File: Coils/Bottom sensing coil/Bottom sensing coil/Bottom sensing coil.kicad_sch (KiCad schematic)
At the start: 6 parts, among them J1 Conn_01x02_Socket, J2 Conn_01x02_Pin

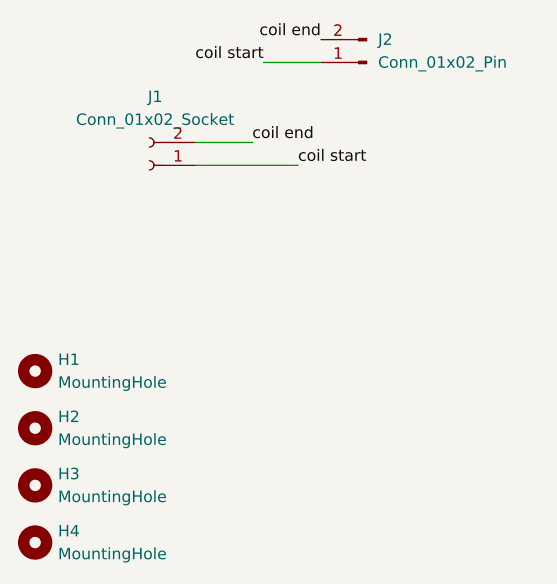
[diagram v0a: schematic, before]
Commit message: added 3d models for OPA3692, THS3091 and BNC connector
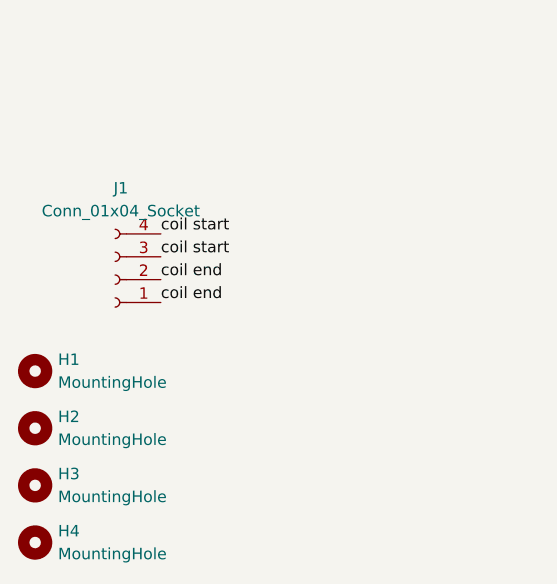
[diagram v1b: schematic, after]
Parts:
- removed J1: Conn_01x02_Socket, Connector_PinSocket_2.54mm:PinSocket_1x02_P2.54mm_Vertical, symbol Connector:Conn_01x02_Socket
- removed J2: Conn_01x02_Pin, Connector_PinHeader_2.54mm:PinHeader_1x02_P2.54mm_Vertical, symbol Connector:Conn_01x02_Pin
- added J1: Conn_01x04_Socket, Connector_PinSocket_2.54mm:PinSocket_1x04_P2.54mm_Horizontal, symbol Connector:Conn_01x04_Socket
- H1, H2, H3, H4: footprint MountingHole:MountingHole_5mm_Pad -> MountingHole:MountingHole_3.2mm_M3_Pad
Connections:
- net coil end: now also J1.1 (Pin_1), J1.2 (Pin_2)
- net coil start: now also J1.3 (Pin_3), J1.4 (Pin_4)
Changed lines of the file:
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@@
 	(generator_version "8.0")
 	(paper "A4")
-	(wire
-		(pts
-			(xy 101.6 55.88) (xy 113.03 55.88)
-		)
-		(stroke
-			(width 0)
-			(type default)
-		)
-	)
-	(wire
-		(pts
-			(xy 115.57 44.45) (xy 109.22 44.45)
-		)
-		(stroke
-			(width 0)
-			(type default)
-		)
-	)
-	(wire
-		(pts
-			(xy 101.6 53.34) (xy 107.95 53.34)
-		)
-		(stroke
-			(width 0)
-			(type default)
-		)
-	)
-	(label "coil end"
-		(at 115.57 41.91 180)
+	(label "coil start"
+		(at 97.79 66.04 0)
 		(fields_autoplaced yes)
 		(effects
@@
 				(size 1.27 1.27)
 			)
-			(justify right bottom)
+			(justify left bottom)
 		)
 	)
 	(label "coil end"
-		(at 107.95 53.34 0)
+		(at 97.79 71.12 0)
 		(fields_autoplaced yes)
 		(effects
@@
 		)
 	)
-	(label "coil start"
-		(at 113.03 55.88 0)
+	(label "coil end"
+		(at 97.79 68.58 0)
 		(fields_autoplaced yes)
 		(effects
@@
 	)
 	(label "coil start"
-		(at 109.22 44.45 180)
+		(at 97.79 63.5 0)
 		(fields_autoplaced yes)
 		(effects
@@
 				(size 1.27 1.27)
 			)
-			(justify right bottom)
+			(justify left bottom)
 		)
 	)
@@
 			)
 		)
-		(property "Footprint" "MountingHole:MountingHole_5mm_Pad"
+		(property "Footprint" "MountingHole:MountingHole_3.2mm_M3_Pad"
 			(at 83.82 91.44 0)
 			(effects
@@
 	)
 	(symbol
-		(lib_id "Connector:Conn_01x02_Pin")
-		(at 120.65 44.45 180)
-		(unit 1)
-		(exclude_from_sim no)
-		(in_bom yes)
-		(on_board yes)
-		(dnp no)
-		(fields_autoplaced yes)
-		(property "Reference" "J2"
-			(at 121.92 41.9099 0)
-			(effects
-				(font
-					(size 1.27 1.27)
-				)
-				(justify right)
-			)
-		)
-		(property "Value" "Conn_01x02_Pin"
-			(at 121.92 44.4499 0)
-			(effects
-				(font
-					(size 1.27 1.27)
-				)
-				(justify right)
-			)
-		)
-		(property "Footprint" "Connector_PinHeader_2.54mm:PinHeader_1x02_P2.54mm_Vertical"
-			(at 120.65 44.45 0)
-			(effects
-				(font
-					(size 1.27 1.27)
-				)
-				(hide yes)
-			)
-		)
-		(property "Datasheet" "~"
-			(at 120.65 44.45 0)
-			(effects
-				(font
-					(size 1.27 1.27)
-				)
-				(hide yes)
-			)
-		)
-		(property "Description" "Generic connector, single row, 01x02, script generated"
-			(at 120.65 44.45 0)
-			(effects
-				(font
-					(size 1.27 1.27)
-				)
-				(hide yes)
-			)
-		)
-		(pin "1"
-		)
-		(pin "2"
-		)
-		(instances
-			(project "Bottom sensing coil"
-				(path "/38c91b10-5af9-4b32-b547-d33c3020bbb1"
-					(reference "J2")
-					(unit 1)
-				)
-			)
-		)
-	)
-	(symbol
 		(lib_id "Mechanical:MountingHole")
 		(at 83.82 85.09 0)
@@
 			)
 		)
-		(property "Footprint" "MountingHole:MountingHole_5mm_Pad"
+		(property "Footprint" "MountingHole:MountingHole_3.2mm_M3_Pad"
 			(at 83.82 85.09 0)
 			(effects
@@
 			)
 		)
-		(property "Footprint" "MountingHole:MountingHole_5mm_Pad"
+		(property "Footprint" "MountingHole:MountingHole_3.2mm_M3_Pad"
 			(at 83.82 97.79 0)
 			(effects
@@
 	)
 	(symbol
-		(lib_id "Connector:Conn_01x02_Socket")
-		(at 96.52 55.88 180)
+		(lib_id "Connector:Conn_01x04_Socket")
+		(at 92.71 68.58 180)
 		(unit 1)
 		(exclude_from_sim no)
@@
 		(fields_autoplaced yes)
 		(property "Reference" "J1"
-			(at 97.155 48.26 0)
-			(effects
-				(font
-					(size 1.27 1.27)
-				)
-			)
-		)
-		(property "Value" "Conn_01x02_Socket"
-			(at 97.155 50.8 0)
-			(effects
-				(font
-					(size 1.27 1.27)
-				)
-			)
-		)
-		(property "Footprint" "Connector_PinSocket_2.54mm:PinSocket_1x02_P2.54mm_Vertical"
-			(at 96.52 55.88 0)
+			(at 93.345 58.42 0)
+			(effects
+				(font
+					(size 1.27 1.27)
+				)
+			)
+		)
+		(property "Value" "Conn_01x04_Socket"
+			(at 93.345 60.96 0)
+			(effects
+				(font
+					(size 1.27 1.27)
+				)
+			)
+		)
+		(property "Footprint" "Connector_PinSocket_2.54mm:PinSocket_1x04_P2.54mm_Horizontal"
+			(at 92.71 68.58 0)
 			(effects
 				(font
@@
 		)
 		(property "Datasheet" "~"
-			(at 96.52 55.88 0)
-			(effects
-				(font
-					(size 1.27 1.27)
-				)
-				(hide yes)
-			)
-		)
-		(property "Description" "Generic connector, single row, 01x02, script generated"
-			(at 96.52 55.88 0)
+			(at 92.71 68.58 0)
+			(effects
+				(font
+					(size 1.27 1.27)
+				)
+				(hide yes)
+			)
+		)
+		(property "Description" "Generic connector, single row, 01x04, script generated"
+			(at 92.71 68.58 0)
 			(effects
 				(font
@@
 		(pin "1"
 		)
+		(pin "4"
+		)
 		(pin "2"
+		)
+		(pin "3"
 		)
 		(instances
@@
 			)
 		)
-		(property "Footprint" "MountingHole:MountingHole_5mm_Pad"
+		(property "Footprint" "MountingHole:MountingHole_3.2mm_M3_Pad"
 			(at 83.82 78.74 0)
 			(effects

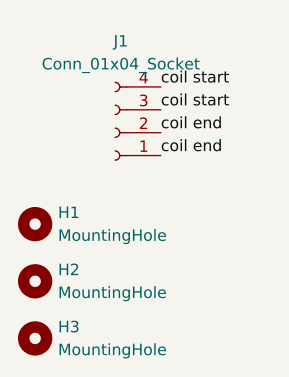
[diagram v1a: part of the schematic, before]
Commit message: Added via stiching to TX board, moved almost all vias off of pads, increased the trace width for the power supply and changed coil connector to horizontal socket
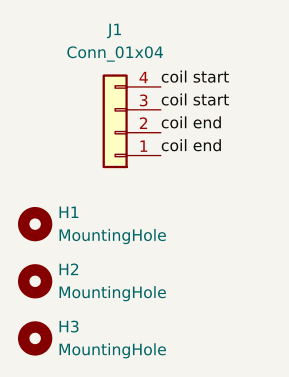
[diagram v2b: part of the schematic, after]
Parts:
- removed J1: Conn_01x04_Socket, Connector_PinSocket_2.54mm:PinSocket_1x04_P2.54mm_Horizontal, symbol Connector:Conn_01x04_Socket
- added J1: Conn_01x04, Connector_PinHeader_2.54mm:PinHeader_1x04_P2.54mm_Horizontal, symbol Connector_Generic:Conn_01x04
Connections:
- net coil end: now also J1.1 (Pin_1), J1.2 (Pin_2)
- net coil start: now also J1.3 (Pin_3), J1.4 (Pin_4)
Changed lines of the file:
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@@
 	)
 	(symbol
-		(lib_id "Connector:Conn_01x04_Socket")
+		(lib_id "Connector_Generic:Conn_01x04")
 		(at 92.71 68.58 180)
 		(unit 1)
@@
 		(fields_autoplaced yes)
 		(property "Reference" "J1"
-			(at 93.345 58.42 0)
+			(at 92.71 57.15 0)
 			(effects
 				(font
@@
 			)
 		)
-		(property "Value" "Conn_01x04_Socket"
-			(at 93.345 60.96 0)
+		(property "Value" "Conn_01x04"
+			(at 92.71 59.69 0)
 			(effects
 				(font
@@
 			)
 		)
-		(property "Footprint" "Connector_PinSocket_2.54mm:PinSocket_1x04_P2.54mm_Horizontal"
+		(property "Footprint" "Connector_PinHeader_2.54mm:PinHeader_1x04_P2.54mm_Horizontal"
 			(at 92.71 68.58 0)
 			(effects
@@
 			)
 		)
-		(property "Description" "Generic connector, single row, 01x04, script generated"
+		(property "Description" "Generic connector, single row, 01x04, script generated (kicad-library-utils/schlib/autogen/connector/)"
 			(at 92.71 68.58 0)
 			(effects
@@
 			)
 		)
-		(pin "1"
+		(pin "2"
 		)
 		(pin "4"
 		)
-		(pin "2"
-		)
 		(pin "3"
 		)
+		(pin "1"
+		)
 		(instances
